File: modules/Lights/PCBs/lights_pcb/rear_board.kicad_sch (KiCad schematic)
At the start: 26 parts, among them J9 Eurorack_2x8_Power, U1 MCP6004, U2 SN74LVC1G3157DCKR, U5 LM4040BIZ-5

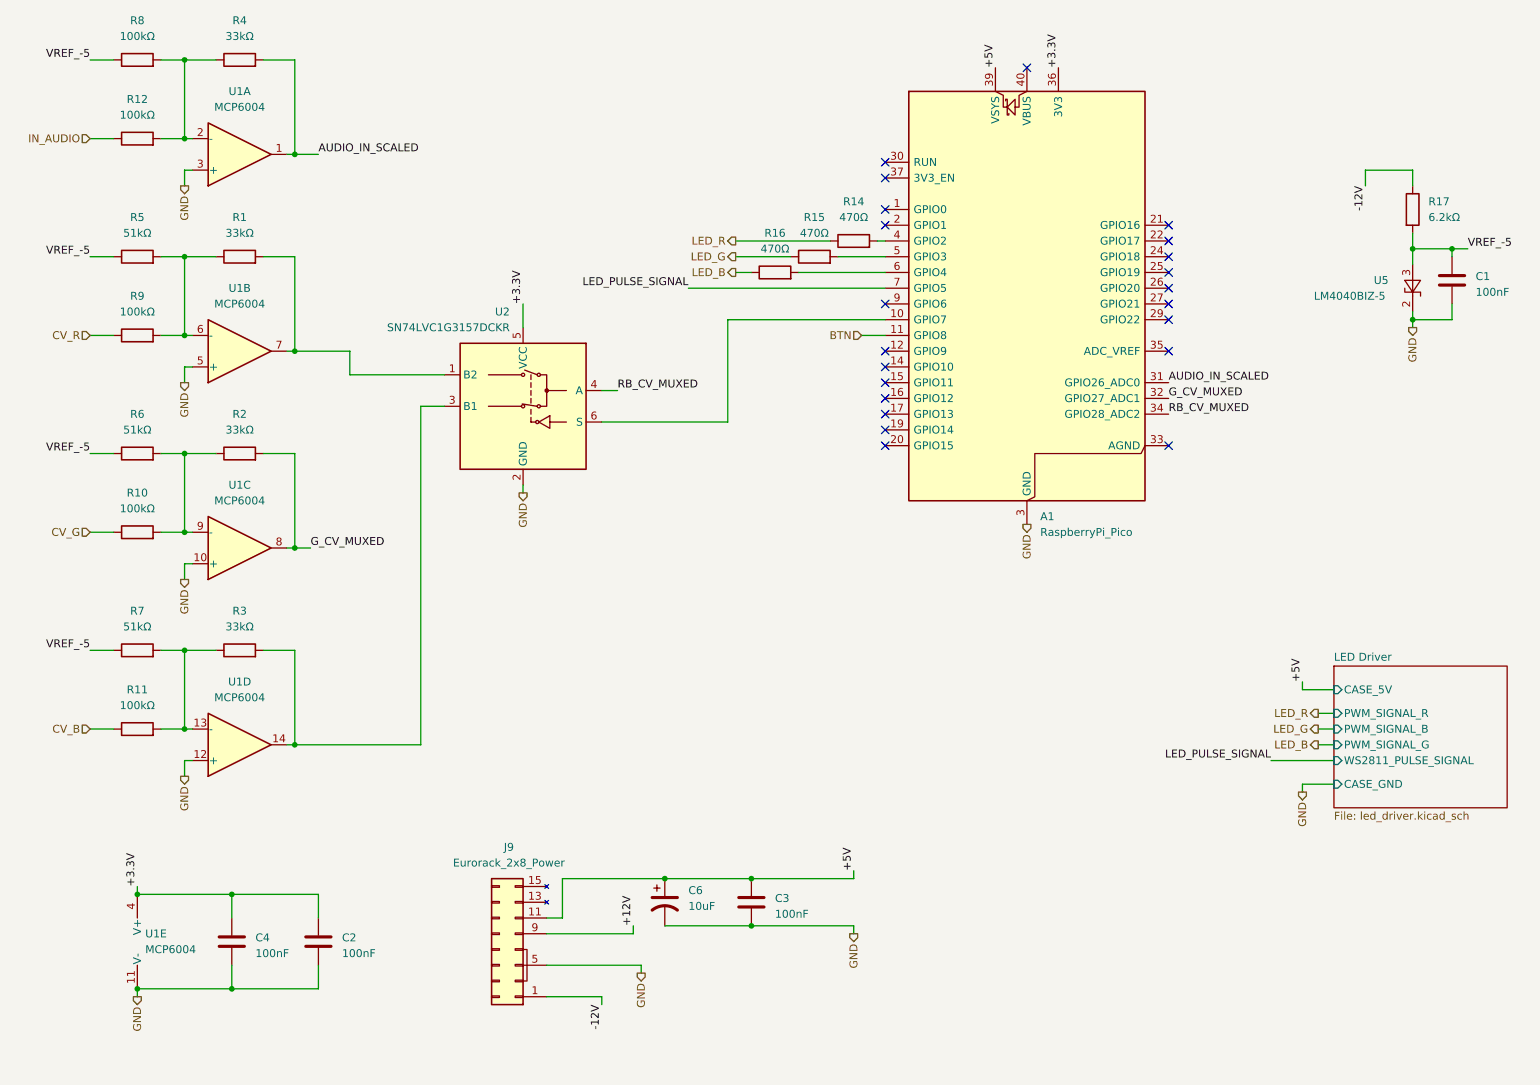
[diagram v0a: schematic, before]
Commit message: Switch lights to external 3.3V power supply instead of using rpi pico
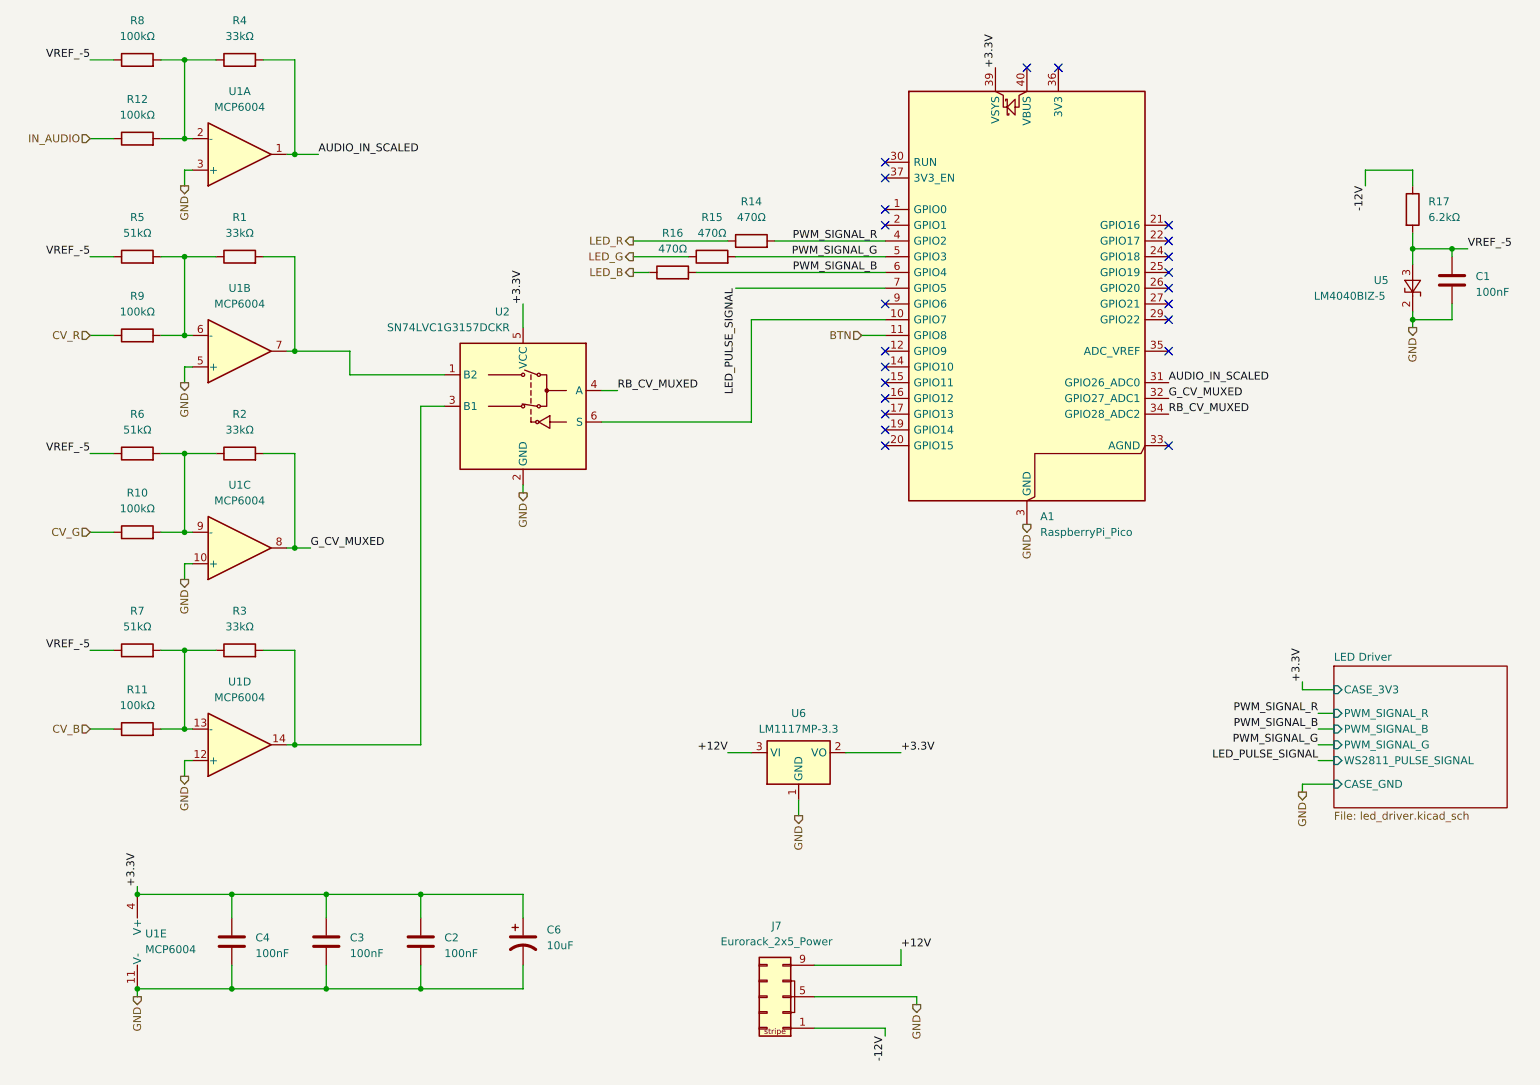
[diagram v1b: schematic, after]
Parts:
- removed J9: Eurorack_2x8_Power, Connector_PinSocket_2.54mm:PinSocket_2x08_P2.54mm_Horizontal, symbol FreeModular:Eurorack_2x8_Power
- added J7: Eurorack_2x5_Power, Connector_IDC:IDC-Header_2x05_P2.54mm_Vertical, symbol FreeModular:Eurorack_2x5_Power
- added U6: LM1117MP-3.3, Package_TO_SOT_SMD:SOT-223-3_TabPin2, symbol Regulator_Linear:LM1117MP-3.3
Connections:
- net +5V is gone; now on net +3.3V: A1.39 (VSYS), C3.1, C6.1
- net +12V: now also J7.10 (+12v), J7.9 (+12v), U6.3 (VI)
- net +3.3V: now also U6.2 (VO); no longer A1.36 (3V3)
- net -12V: now also J7.1 (-12v), J7.2 (-12v)
- net GND: now also J7.3 (GND), J7.4 (GND), J7.5 (GND), J7.6 (GND), J7.7 (GND), J7.8 (GND), U6.1 (GND)
- net PWM_SIGNAL_R: now reaches A1.4 (GPIO2), R14.2
- net PWM_SIGNAL_G: now reaches A1.5 (GPIO3), R15.2
- net PWM_SIGNAL_B: now reaches A1.6 (GPIO4), R16.2
- no-connect marks 22 -> 23
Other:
- sheet LED Driver ports: added CASE_3V3; removed CASE_5V
- moved on the sheet: C2, C3, C6, R14, R15, R16
